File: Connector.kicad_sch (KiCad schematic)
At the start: 3 parts

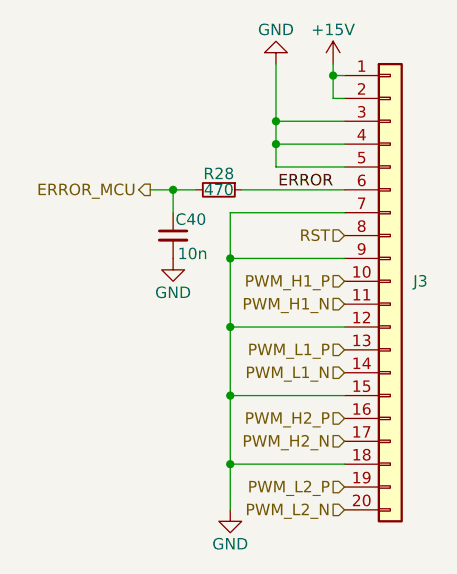
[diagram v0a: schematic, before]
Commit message: VER1.0: добавил разделение питания VDD и VDDA
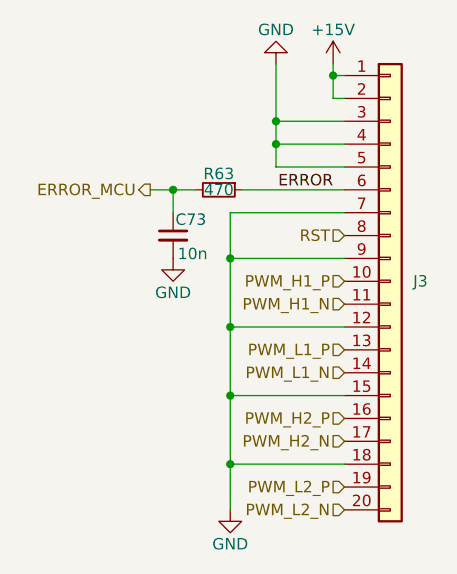
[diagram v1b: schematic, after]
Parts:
- C73: renamed from C40; Description P/N (none) -> Capacitor SMD 25V
- R63: renamed from R28; Description P/N (none) -> Resistor SMD 1%
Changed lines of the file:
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@@
 		(in_pos_files yes)
 		(dnp no)
-		(property "Reference" "C40"
+		(property "Reference" "C73"
 			(at 136.144 87.122 0)
 			(show_name no)
@@
 			)
 		)
-		(property "Purpose" ""
-			(at 135.89 88.9 0)
-			(hide yes)
-			(show_name no)
-			(do_not_autoplace no)
-			(effects
-				(font
-					(size 1.27 1.27)
-				)
-			)
-		)
-		(property "Description P/N" ""
+		(property "Description P/N" "Capacitor SMD 25V"
 			(at 135.89 88.9 0)
 			(hide yes)
@@
 			(project "PSFB_MCU"
 				(path "/1f44d793-713f-4781-bd7e-20142de81965/70828a48-f97b-4e66-8746-e00d52ef0e18"
-					(reference "C40")
+					(reference "C73")
 					(unit 1)
 				)
 				(path "/1f44d793-713f-4781-bd7e-20142de81965/a38d4a25-54b0-402f-ba25-3bfc3756c343"
-					(reference "C57")
+					(reference "C74")
 					(unit 1)
 				)
@@
 		(in_pos_files yes)
 		(dnp no)
-		(property "Reference" "#PWR088"
+		(property "Reference" "#PWR0195"
 			(at 153.67 73.66 0)
 			(hide yes)
@@
 			(project "PSFB_MCU"
 				(path "/1f44d793-713f-4781-bd7e-20142de81965/70828a48-f97b-4e66-8746-e00d52ef0e18"
-					(reference "#PWR088")
+					(reference "#PWR0195")
 					(unit 1)
 				)
 				(path "/1f44d793-713f-4781-bd7e-20142de81965/a38d4a25-54b0-402f-ba25-3bfc3756c343"
-					(reference "#PWR0165")
+					(reference "#PWR0199")
 					(unit 1)
 				)
@@
 		(in_pos_files yes)
 		(dnp no)
-		(property "Reference" "#PWR087"
+		(property "Reference" "#PWR0197"
 			(at 142.24 125.73 0)
 			(hide yes)
@@
 			(project "PSFB_MCU"
 				(path "/1f44d793-713f-4781-bd7e-20142de81965/70828a48-f97b-4e66-8746-e00d52ef0e18"
-					(reference "#PWR087")
+					(reference "#PWR0197")
 					(unit 1)
 				)
 				(path "/1f44d793-713f-4781-bd7e-20142de81965/a38d4a25-54b0-402f-ba25-3bfc3756c343"
-					(reference "#PWR0163")
+					(reference "#PWR0201")
 					(unit 1)
 				)
@@
 		(in_pos_files yes)
 		(dnp no)
-		(property "Reference" "#PWR096"
+		(property "Reference" "#PWR0196"
 			(at 135.89 97.79 0)
 			(hide yes)
@@
 			(project "PSFB_MCU"
 				(path "/1f44d793-713f-4781-bd7e-20142de81965/70828a48-f97b-4e66-8746-e00d52ef0e18"
-					(reference "#PWR096")
+					(reference "#PWR0196")
 					(unit 1)
 				)
 				(path "/1f44d793-713f-4781-bd7e-20142de81965/a38d4a25-54b0-402f-ba25-3bfc3756c343"
-					(reference "#PWR0162")
+					(reference "#PWR0200")
 					(unit 1)
 				)
@@
 			)
 		)
-		(property "Datasheet" "FH12-20S-0.5SH"
+		(property "Datasheet" ""
 			(at 160.02 93.98 0)
 			(hide yes)
@@
 		(in_pos_files yes)
 		(dnp no)
-		(property "Reference" "R28"
+		(property "Reference" "R63"
 			(at 140.97 82.042 90)
 			(show_name no)
@@
 			)
 		)
-		(property "Purpose" ""
-			(at 140.97 83.82 0)
-			(hide yes)
-			(show_name no)
-			(do_not_autoplace no)
-			(effects
-				(font
-					(size 1.27 1.27)
-				)
-			)
-		)
-		(property "Description P/N" ""
+		(property "Description P/N" "Resistor SMD 1%"
 			(at 140.97 83.82 0)
 			(hide yes)
@@
 			(project "PSFB_MCU"
 				(path "/1f44d793-713f-4781-bd7e-20142de81965/70828a48-f97b-4e66-8746-e00d52ef0e18"
-					(reference "R28")
+					(reference "R63")
 					(unit 1)
 				)
 				(path "/1f44d793-713f-4781-bd7e-20142de81965/a38d4a25-54b0-402f-ba25-3bfc3756c343"
-					(reference "R47")
+					(reference "R64")
 					(unit 1)
 				)
@@
 		(in_pos_files yes)
 		(dnp no)
-		(property "Reference" "#PWR0161"
+		(property "Reference" "#PWR0194"
 			(at 147.32 63.5 0)
 			(hide yes)
@@
 			(project "PSFB_MCU"
 				(path "/1f44d793-713f-4781-bd7e-20142de81965/70828a48-f97b-4e66-8746-e00d52ef0e18"
-					(reference "#PWR0161")
+					(reference "#PWR0194")
 					(unit 1)
 				)
 				(path "/1f44d793-713f-4781-bd7e-20142de81965/a38d4a25-54b0-402f-ba25-3bfc3756c343"
-					(reference "#PWR0164")
-					(unit 1)
-				)
+					(reference "#PWR0198")
+					(unit 1)
+				)
